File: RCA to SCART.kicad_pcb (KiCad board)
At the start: 2 copper layers, 42 x 68.3 mm, 10 parts, among them J1 Conn_01x01, J2 Conn_01x01, J3 Conn_01x01, J4 Conn_01x01

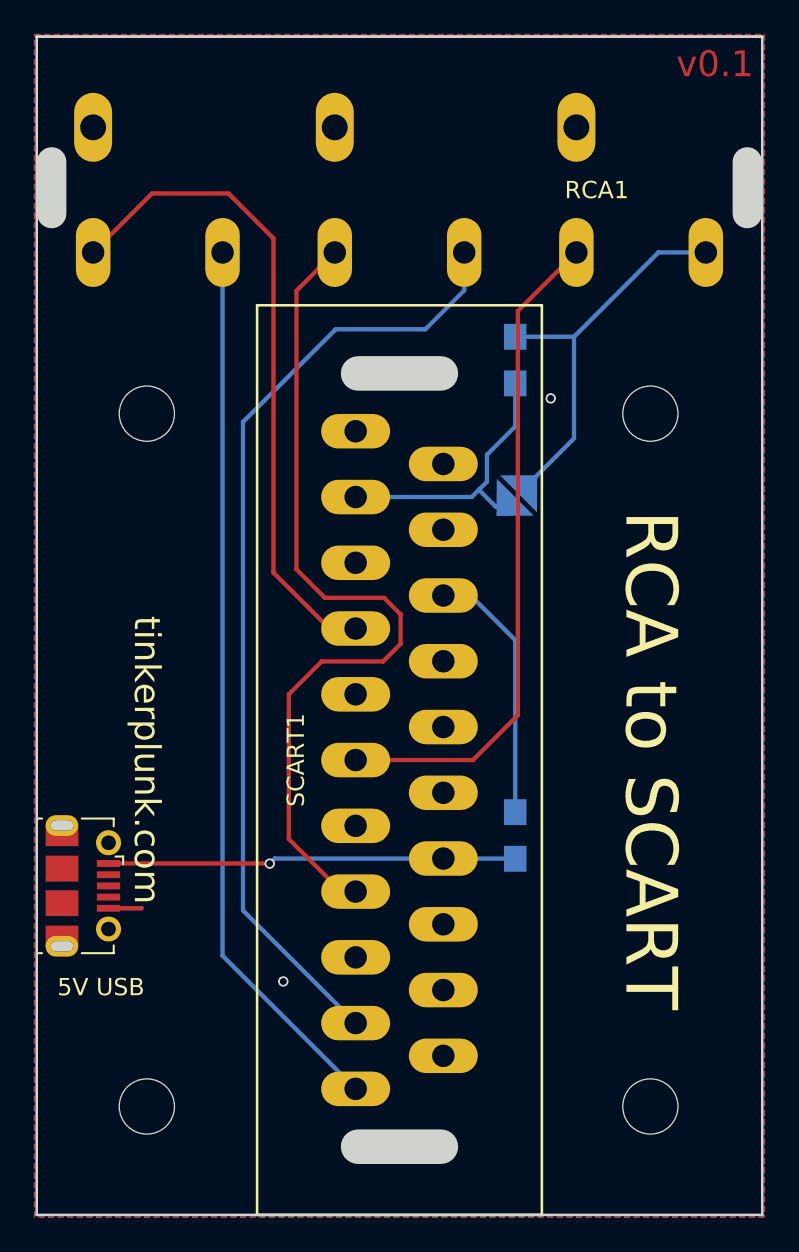
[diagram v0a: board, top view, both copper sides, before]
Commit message: v0.2
0.2 - The shield througholes of the microusb port were not connected to ground, this has been fixed. I also moved a few traces
around to make it easier to disconnect pin 8 if it is causing your TV to force to 16:9.
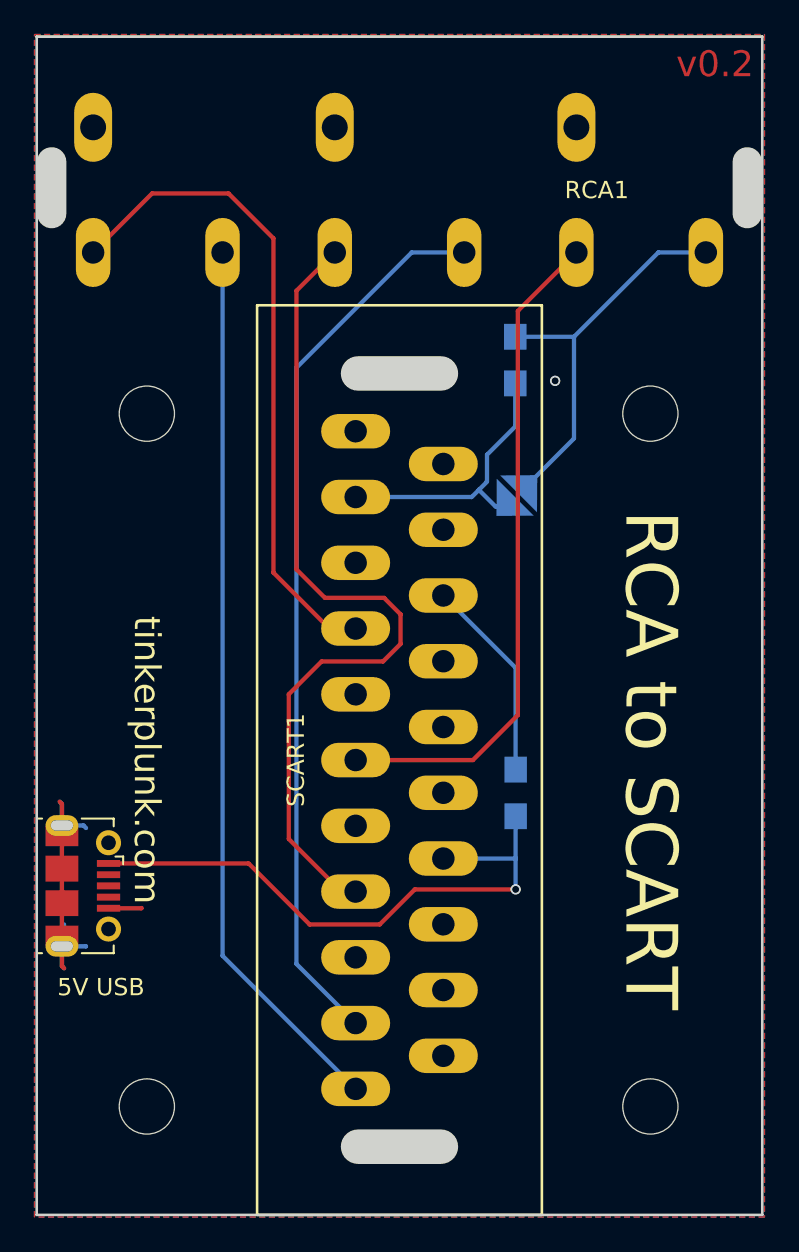
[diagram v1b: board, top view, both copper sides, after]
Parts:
- moved 100Ω 2.46 mm to (157.2, 110.2)
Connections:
- 5V USB pad 6: (no net) -> GND
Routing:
- net GND: track 1.93 -> 19.6 mm, vias 2 -> 1
- net Net-(J5-Pad1): track 23.7 -> 36.1 mm
- net L_AUD: track 55.7 -> 51.9 mm
- net Net-(R1-Pad2): track 15.2 -> 13.4 mm
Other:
- board text added: "v0.2"
- board text removed: "v0.1"
